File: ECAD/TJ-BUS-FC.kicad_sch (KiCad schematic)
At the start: 19 parts

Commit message: changed fram chip
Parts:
- removed C?: 1uF, symbol Device:C
- removed U?: Adafruit_FRAM, symbol Symbols:Adafruit_FRAM
- added C?: (no value), symbol Device:C
- added J?: PWR, symbol Connector:Conn_01x02_Female
- added U?: (no value), symbol Memory_NVRAM:MB85RS64
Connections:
- net +3V3: no longer U?.2 (3vo)
- net CS/GP37: now also U?.1 (~{CS})
- net GND: now also C?.2, J?.2 (Pin_2), U?.4 (GND)
- net MOSI0: now also U?.5 (SI)
- net SCK0: now also U?.6 (SCK)
- net SCL0: now also U?.5 (SCL)
- net SCL1: no longer U?.5 (SCL)
- net SDA0: now also U?.4 (SDA)
- net SDA1: no longer U?.4 (SDA)
- net 5VIN: now reaches H1.32 (Pin_32)
- net 5VIN: now also J?.1 (Pin_1)
- net at U?.46 (3V3): now also C?.1, U?.8 (VDD)
- new net MOSO0: U?.2 (SO)
- no-connect marks 19 -> 18
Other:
- moved on the sheet: U?

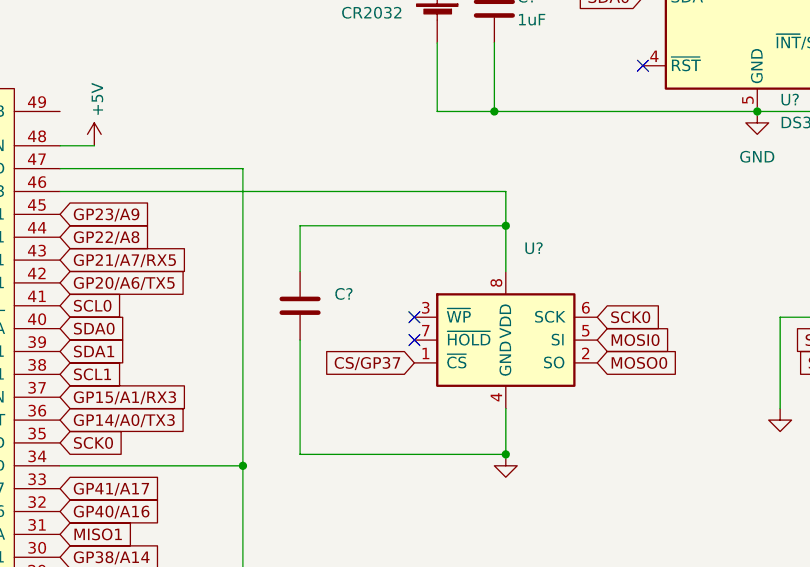
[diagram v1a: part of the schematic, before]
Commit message: set low activated pins to high
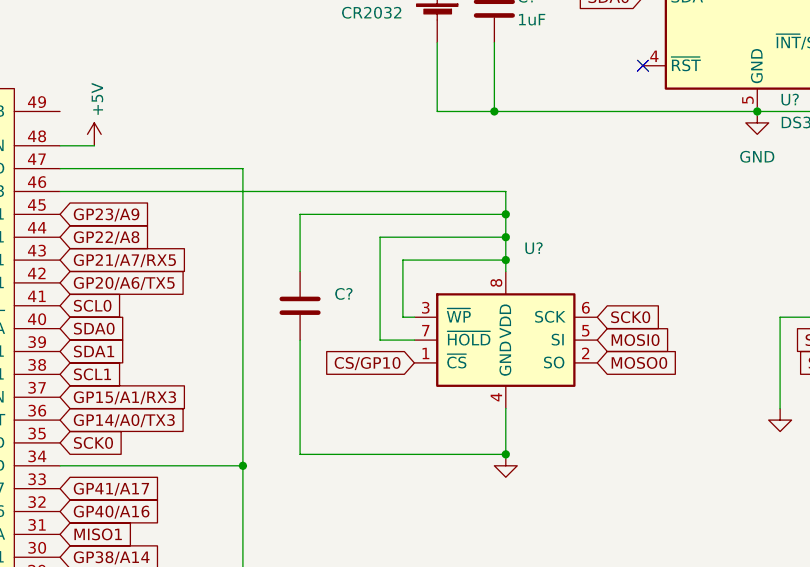
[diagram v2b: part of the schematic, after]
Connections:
- net CS/GP10: now also U?.1 (~{CS})
- net CS/GP37: no longer U?.1 (~{CS})
- net at U?.3 (~{WP}): now also C?.1, U?.46 (3V3), U?.7 (~{HOLD}), U?.8 (VDD)
- no-connect marks 18 -> 16
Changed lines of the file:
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@@
 (kicad_sch (version 20211123) (generator eeschema)
   (paper "USLegal")
-  (junction (at 165.1 64.77) (diameter 0) (color 0 0 0 0)
+  (junction (at 165.1 63.5) (diameter 0) (color 0 0 0 0)
+  )
+  (junction (at 165.1 66.04) (diameter 0) (color 0 0 0 0)
   )
   (junction (at 336.55 86.36) (diameter 0) (color 0 0 0 0)
@@
   )
   (junction (at 306.07 86.36) (diameter 0) (color 0 0 0 0)
+  )
+  (junction (at 165.1 68.58) (diameter 0) (color 0 0 0 0)
   )
   (junction (at 193.04 52.07) (diameter 0) (color 0 0 0 0)
@@
   (no_connect (at 204.47 72.39))
   (no_connect (at 224.79 80.01))
-  (no_connect (at 154.94 74.93))
   (no_connect (at 224.79 74.93))
   (no_connect (at 224.79 72.39))
@@
   (no_connect (at 327.66 96.52))
   (no_connect (at 327.66 76.2))
-  (no_connect (at 154.94 77.47))
   (wire (pts (xy 115.57 123.19) (xy 135.89 123.19))
     (stroke (width 0) (type default) (color 0 0 0 0))
   )
+  (wire (pts (xy 153.67 68.58) (xy 153.67 74.93))
+    (stroke (width 0) (type default) (color 0 0 0 0))
+  )
   (wire (pts (xy 163.83 31.75) (xy 163.83 36.83))
     (stroke (width 0) (type default) (color 0 0 0 0))
@@
     (stroke (width 0) (type default) (color 0 0 0 0))
   )
+  (wire (pts (xy 165.1 68.58) (xy 165.1 69.85))
+    (stroke (width 0) (type default) (color 0 0 0 0))
+  )
   (wire (pts (xy 157.48 52.07) (xy 163.83 52.07))
     (stroke (width 0) (type default) (color 0 0 0 0))
   )
+  (wire (pts (xy 165.1 66.04) (xy 165.1 68.58))
+    (stroke (width 0) (type default) (color 0 0 0 0))
+  )
   (wire (pts (xy 41.91 55.88) (xy 41.91 133.35))
     (stroke (width 0) (type default) (color 0 0 0 0))
@@
     (stroke (width 0) (type default) (color 0 0 0 0))
   )
+  (wire (pts (xy 151.13 66.04) (xy 151.13 77.47))
+    (stroke (width 0) (type default) (color 0 0 0 0))
+  )
   (wire (pts (xy 306.07 83.82) (xy 314.96 83.82))
     (stroke (width 0) (type default) (color 0 0 0 0))
@@
     (stroke (width 0) (type default) (color 0 0 0 0))
   )
+  (wire (pts (xy 154.94 74.93) (xy 153.67 74.93))
+    (stroke (width 0) (type default) (color 0 0 0 0))
+  )
   (wire (pts (xy 115.57 60.96) (xy 165.1 60.96))
     (stroke (width 0) (type default) (color 0 0 0 0))
@@
     (stroke (width 0) (type default) (color 0 0 0 0))
   )
-  (wire (pts (xy 165.1 60.96) (xy 165.1 64.77))
+  (wire (pts (xy 165.1 60.96) (xy 165.1 63.5))
     (stroke (width 0) (type default) (color 0 0 0 0))
   )
@@
     (stroke (width 0) (type default) (color 0 0 0 0))
   )
-  (wire (pts (xy 165.1 64.77) (xy 165.1 69.85))
+  (wire (pts (xy 165.1 63.5) (xy 165.1 66.04))
+    (stroke (width 0) (type default) (color 0 0 0 0))
+  )
+  (wire (pts (xy 153.67 68.58) (xy 165.1 68.58))
     (stroke (width 0) (type default) (color 0 0 0 0))
   )
@@
     (stroke (width 0) (type default) (color 0 0 0 0))
   )
+  (wire (pts (xy 151.13 77.47) (xy 154.94 77.47))
+    (stroke (width 0) (type default) (color 0 0 0 0))
+  )
   (wire (pts (xy 165.1 85.09) (xy 165.1 90.17))
     (stroke (width 0) (type default) (color 0 0 0 0))
@@
     (stroke (width 0) (type default) (color 0 0 0 0))
   )
+  (wire (pts (xy 165.1 66.04) (xy 151.13 66.04))
+    (stroke (width 0) (type default) (color 0 0 0 0))
+  )
   (wire (pts (xy 163.83 31.75) (xy 157.48 31.75))
     (stroke (width 0) (type default) (color 0 0 0 0))
   )
-  (wire (pts (xy 142.24 64.77) (xy 165.1 64.77))
-    (stroke (width 0) (type default) (color 0 0 0 0))
-  )
-  (wire (pts (xy 142.24 69.85) (xy 142.24 64.77))
+  (wire (pts (xy 142.24 63.5) (xy 165.1 63.5))
+    (stroke (width 0) (type default) (color 0 0 0 0))
+  )
+  (wire (pts (xy 142.24 69.85) (xy 142.24 63.5))
     (stroke (width 0) (type default) (color 0 0 0 0))
   )
@@
     )
   )
-  (global_label "CS{slash}GP37" (shape input) (at 154.94 80.01 180) (fields_autoplaced)
+  (global_label "CS{slash}GP10" (shape input) (at 154.94 80.01 180) (fields_autoplaced)
     (effects (font (size 1.27 1.27)) (justify right))
     (property "Intersheet References" "${INTERSHEET_REFS}" (id 0) (at 143.8468 79.9306 0)

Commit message: minor nitpicks
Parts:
- removed J?: PWR, symbol Connector:Conn_01x02_Female
- U?: value (none) -> MB85RS64
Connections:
- net 5VIN: no longer names the net of H1.32 (Pin_32)
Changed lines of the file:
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@@
 (kicad_sch (version 20211123) (generator eeschema)
   (paper "USLegal")
-  (junction (at 165.1 63.5) (diameter 0) (color 0 0 0 0)
-  )
-  (junction (at 165.1 66.04) (diameter 0) (color 0 0 0 0)
-  )
   (junction (at 336.55 86.36) (diameter 0) (color 0 0 0 0)
   )
   (junction (at 165.1 90.17) (diameter 0) (color 0 0 0 0)
   )
+  (junction (at 151.13 74.93) (diameter 0) (color 0 0 0 0)
+  )
   (junction (at 163.83 31.75) (diameter 0) (color 0 0 0 0)
   )
@@
   (junction (at 306.07 86.36) (diameter 0) (color 0 0 0 0)
   )
-  (junction (at 165.1 68.58) (diameter 0) (color 0 0 0 0)
+  (junction (at 142.24 60.96) (diameter 0) (color 0 0 0 0)
   )
   (junction (at 193.04 52.07) (diameter 0) (color 0 0 0 0)
+  )
+  (junction (at 151.13 60.96) (diameter 0) (color 0 0 0 0)
   )
   (no_connect (at 314.96 93.98))
@@
     (stroke (width 0) (type default) (color 0 0 0 0))
   )
-  (wire (pts (xy 153.67 68.58) (xy 153.67 74.93))
+  (wire (pts (xy 151.13 74.93) (xy 151.13 77.47))
     (stroke (width 0) (type default) (color 0 0 0 0))
   )
@@
     (stroke (width 0) (type default) (color 0 0 0 0))
   )
-  (wire (pts (xy 165.1 68.58) (xy 165.1 69.85))
-    (stroke (width 0) (type default) (color 0 0 0 0))
-  )
   (wire (pts (xy 157.48 52.07) (xy 163.83 52.07))
     (stroke (width 0) (type default) (color 0 0 0 0))
   )
-  (wire (pts (xy 165.1 66.04) (xy 165.1 68.58))
-    (stroke (width 0) (type default) (color 0 0 0 0))
-  )
   (wire (pts (xy 41.91 55.88) (xy 41.91 133.35))
     (stroke (width 0) (type default) (color 0 0 0 0))
@@
     (stroke (width 0) (type default) (color 0 0 0 0))
   )
+  (wire (pts (xy 142.24 60.96) (xy 151.13 60.96))
+    (stroke (width 0) (type default) (color 0 0 0 0))
+  )
   (wire (pts (xy 306.07 86.36) (xy 314.96 86.36))
     (stroke (width 0) (type default) (color 0 0 0 0))
@@
     (stroke (width 0) (type default) (color 0 0 0 0))
   )
-  (wire (pts (xy 151.13 66.04) (xy 151.13 77.47))
+  (wire (pts (xy 151.13 60.96) (xy 151.13 74.93))
     (stroke (width 0) (type default) (color 0 0 0 0))
   )
@@
     (stroke (width 0) (type default) (color 0 0 0 0))
   )
-  (wire (pts (xy 154.94 74.93) (xy 153.67 74.93))
-    (stroke (width 0) (type default) (color 0 0 0 0))
-  )
-  (wire (pts (xy 115.57 60.96) (xy 165.1 60.96))
+  (wire (pts (xy 151.13 74.93) (xy 154.94 74.93))
+    (stroke (width 0) (type default) (color 0 0 0 0))
+  )
+  (wire (pts (xy 115.57 60.96) (xy 142.24 60.96))
+    (stroke (width 0) (type default) (color 0 0 0 0))
+  )
+  (wire (pts (xy 151.13 60.96) (xy 165.1 60.96))
     (stroke (width 0) (type default) (color 0 0 0 0))
   )
@@
     (stroke (width 0) (type default) (color 0 0 0 0))
   )
-  (wire (pts (xy 165.1 60.96) (xy 165.1 63.5))
+  (wire (pts (xy 165.1 60.96) (xy 165.1 69.85))
     (stroke (width 0) (type default) (color 0 0 0 0))
   )
@@
     (stroke (width 0) (type default) (color 0 0 0 0))
   )
-  (wire (pts (xy 165.1 63.5) (xy 165.1 66.04))
-    (stroke (width 0) (type default) (color 0 0 0 0))
-  )
-  (wire (pts (xy 153.67 68.58) (xy 165.1 68.58))
-    (stroke (width 0) (type default) (color 0 0 0 0))
-  )
   (wire (pts (xy 157.48 31.75) (xy 157.48 36.83))
     (stroke (width 0) (type default) (color 0 0 0 0))
@@
     (stroke (width 0) (type default) (color 0 0 0 0))
   )
-  (wire (pts (xy 165.1 66.04) (xy 151.13 66.04))
-    (stroke (width 0) (type default) (color 0 0 0 0))
-  )
   (wire (pts (xy 163.83 31.75) (xy 157.48 31.75))
     (stroke (width 0) (type default) (color 0 0 0 0))
   )
-  (wire (pts (xy 142.24 63.5) (xy 165.1 63.5))
-    (stroke (width 0) (type default) (color 0 0 0 0))
-  )
-  (wire (pts (xy 142.24 69.85) (xy 142.24 63.5))
+  (wire (pts (xy 142.24 60.96) (xy 142.24 69.85))
     (stroke (width 0) (type default) (color 0 0 0 0))
   )
@@
     )
   )
-  (global_label "5VIN" (shape input) (at 224.79 135.89 180) (fields_autoplaced)
-    (effects (font (size 1.27 1.27)) (justify right))
-    (property "Intersheet References" "${INTERSHEET_REFS}" (id 0) (at 462.28 220.98 0)
-      (effects (font (size 1.27 1.27)) hide)
-    )
-  )
   (global_label "RX2{slash}GP7" (shape input) (at 279.4 58.42 180) (fields_autoplaced)
     (effects (font (size 1.27 1.27)) (justify right))
@@
     (property "Intersheet References" "${INTERSHEET_REFS}" (id 0) (at 304.2213 78.6606 0)
       (effects (font (size 1.27 1.27)) (justify left) hide)
-    )
-  )
-  (global_label "5VIN" (shape input) (at 292.1 86.36 0) (fields_autoplaced)
-    (effects (font (size 1.27 1.27)) (justify left))
-    (property "Intersheet References" "${INTERSHEET_REFS}" (id 0) (at 54.61 1.27 0)
-      (effects (font (size 1.27 1.27)) hide)
     )
   )
@@
       (effects (font (size 1.27 1.27)) hide)
     )
-    (property "Value" "" (id 1) (at 195.58 90.17 0))
+    (property "Value" "GND" (id 1) (at 195.58 90.17 0))
     (property "Footprint" "" (id 2) (at 195.58 85.09 0)
       (effects (font (size 1.27 1.27)) hide)
@@
       (effects (font (size 1.27 1.27)) (justify left))
     )
-    (property "Value" "" (id 1) (at 167.1194 69.85 0)
+    (property "Value" "MB85RS64" (id 1) (at 167.1194 69.85 0)
       (effects (font (size 1.27 1.27)) (justify left))
     )
@@
     (pin "8")
   )
-  (symbol (lib_id "Connector:Conn_01x02_Female") (at 229.87 135.89 0) (unit 1)
-    (in_bom yes) (on_board yes) (fields_autoplaced)
-    (property "Reference" "J?" (id 0) (at 231.14 135.8899 0)
-      (effects (font (size 1.27 1.27)) (justify left))
-    )
-    (property "Value" "PWR" (id 1) (at 231.14 138.4299 0)
-      (effects (font (size 1.27 1.27)) (justify left))
-    )
-    (property "Footprint" "" (id 2) (at 229.87 135.89 0)
-      (effects (font (size 1.27 1.27)) hide)
-    )
-    (property "Datasheet" "~" (id 3) (at 229.87 135.89 0)
-      (effects (font (size 1.27 1.27)) hide)
-    )
-    (pin "1")
-    (pin "2")
-  )
   (symbol (lib_id "power:GND") (at 193.04 52.07 0) (unit 1)
     (in_bom yes) (on_board yes)
@@
     (pin "1")
   )
-  (symbol (lib_id "power:GND") (at 224.79 138.43 0) (unit 1)
-    (in_bom yes) (on_board yes) (fields_autoplaced)
-    (property "Reference" "#PWR?" (id 0) (at 224.79 144.78 0)
-      (effects (font (size 1.27 1.27)) hide)
-    )
-    (property "Value" "GND" (id 1) (at 224.79 143.51 0))
-    (property "Footprint" "" (id 2) (at 224.79 138.43 0)
-      (effects (font (size 1.27 1.27)) hide)
-    )
-    (property "Datasheet" "" (id 3) (at 224.79 138.43 0)
-      (effects (font (size 1.27 1.27)) hide)
-    )
-    (pin "1")
-  )
   (symbol (lib_id "Device:C") (at 163.83 40.64 0) (unit 1)
     (in_bom yes) (on_board yes)
@@
       (effects (font (size 1.27 1.27)) hide)
     )
-    (property "Value" "" (id 1) (at 165.1 95.25 0))
+    (property "Value" "GND" (id 1) (at 165.1 95.25 0))
     (property "Footprint" "" (id 2) (at 165.1 90.17 0)
       (effects (font (size 1.27 1.27)) hide)
@@
   )
   (symbol (lib_id "Device:C") (at 142.24 73.66 0) (unit 1)
-    (in_bom yes) (on_board yes) (fields_autoplaced)
-    (property "Reference" "C?" (id 0) (at 146.05 72.3899 0)
-      (effects (font (size 1.27 1.27)) (justify left))
-    )
-    (property "Value" "" (id 1) (at 146.05 74.9299 0)
+    (in_bom yes) (on_board yes)
+    (property "Reference" "C?" (id 0) (at 144.78 72.39 0)
+      (effects (font (size 1.27 1.27)) (justify left))
+    )
+    (property "Value" "" (id 1) (at 144.78 74.93 0)
       (effects (font (size 1.27 1.27)) (justify left))
     )
@@
       (effects (font (size 1.27 1.27)) hide)
     )
-    (property "Value" "" (id 1) (at 200.66 69.8499 90)
+    (property "Value" "+3.3V" (id 1) (at 200.66 69.8499 90)
       (effects (font (size 1.27 1.27)) (justify left))
     )
@@
       (reference "#PWR?") (unit 1) (value "GND") (footprint "")
     )
-    (path "/ada2bafc-40cb-4d29-9269-ce160ab48fcc"
-      (reference "#PWR?") (unit 1) (value "GND") (footprint "")
-    )
     (path "/1b0ebad7-8a43-40a6-b997-58eed2589c95/ba16728d-3684-42ae-a4d8-298c4a006593"
       (reference "#PWR?") (unit 1) (value "GND") (footprint "")
@@
     )
     (path "/be5f9a77-0429-4df0-92dd-b6e55cb3b5d6"
-      (reference "C?") (unit 1) (value "1uF") (footprint "")
+      (reference "C?") (unit 1) (value "0.1uF") (footprint "")
     )
     (path "/1b0ebad7-8a43-40a6-b997-58eed2589c95/c8117bba-6b2a-4528-9104-16037ce7eb42"
@@
       (reference "H2") (unit 1) (value "Stack Header") (footprint "Connector_PinHeader_2.54mm:PinHeader_2x26_P2.54mm_Vertical")
     )
-    (path "/8142001c-a9d5-457a-9968-95120d035d39"
-      (reference "J?") (unit 1) (value "PWR") (footprint "")
-    )
     (path "/1b0ebad7-8a43-40a6-b997-58eed2589c95/2c8c9572-9c16-41b9-81dc-5ea6c5fa6361"

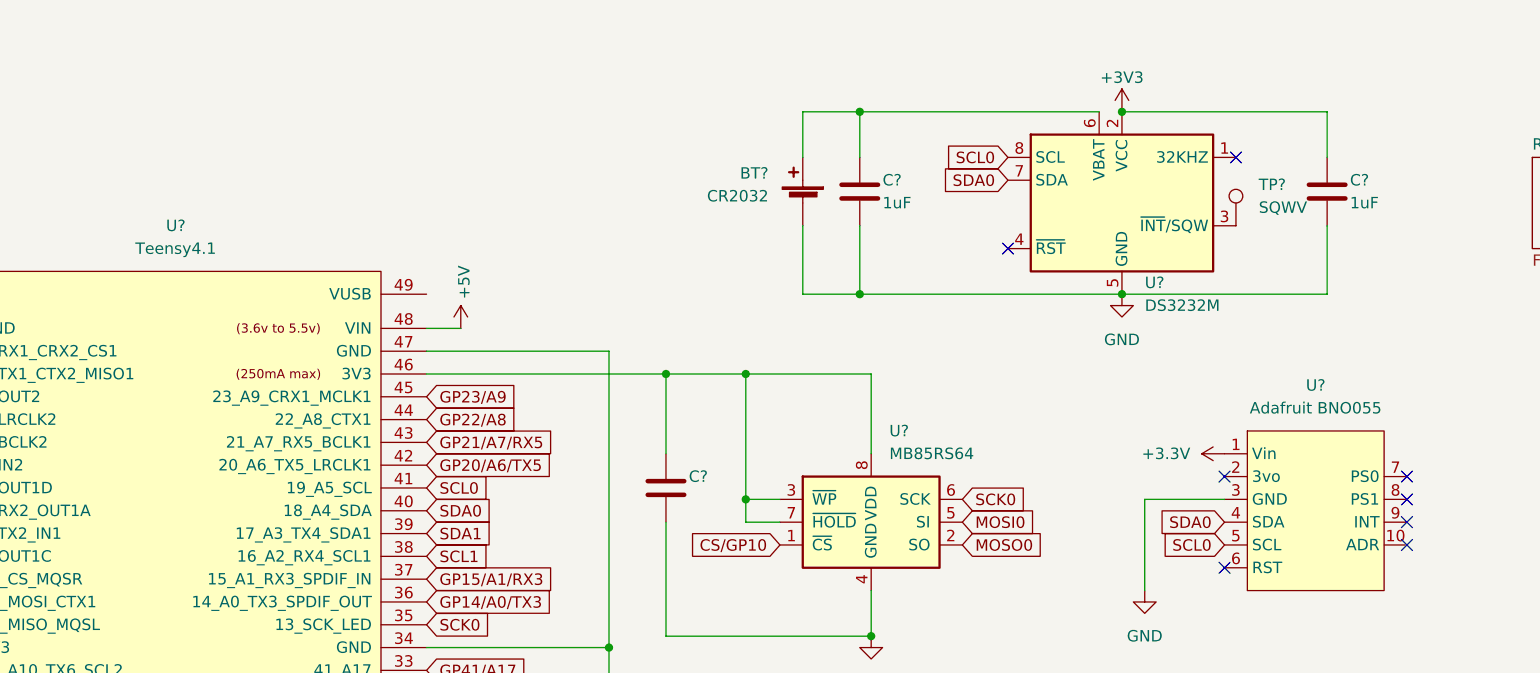
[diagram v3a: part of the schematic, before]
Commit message: add footprints and update iridium section
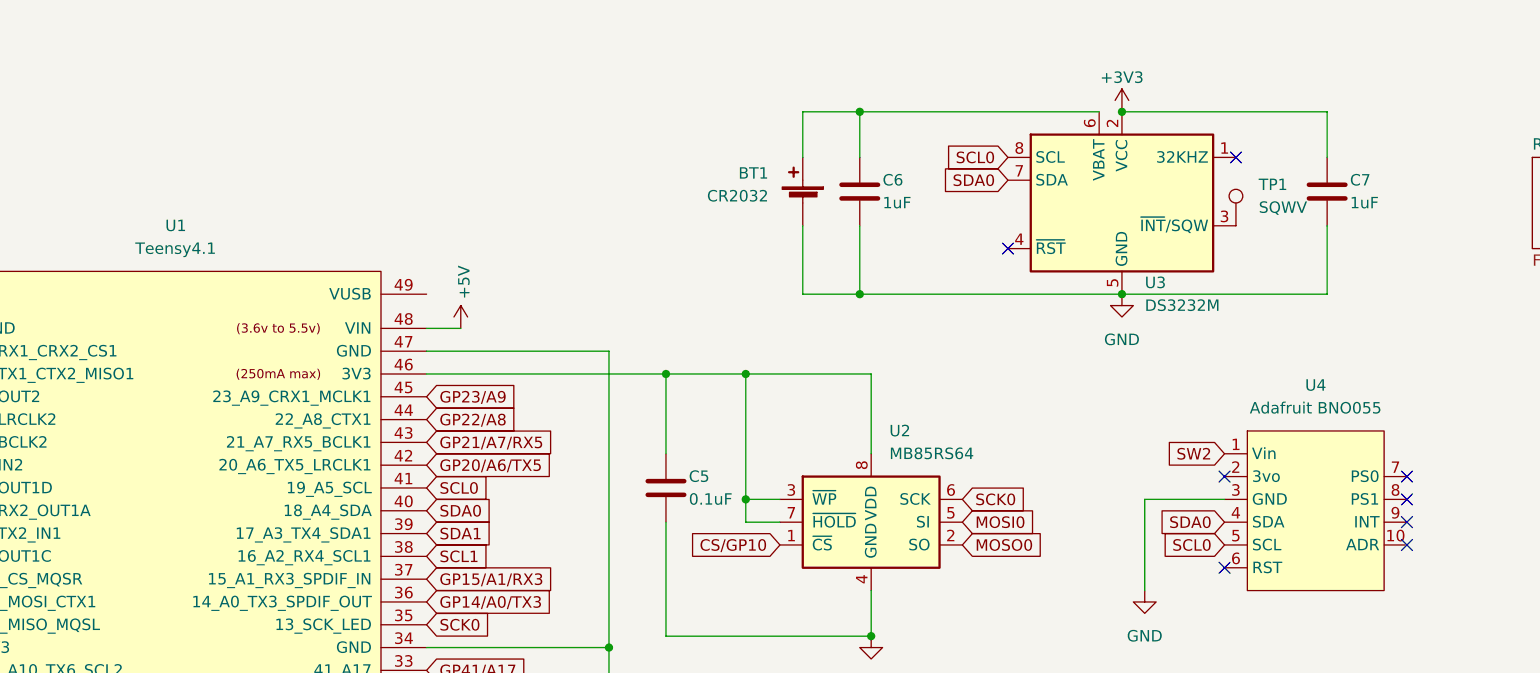
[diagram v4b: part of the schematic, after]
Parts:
- C5: renamed from C?; value (none) -> 0.1uF
- gave numbers to parts that had none: 8
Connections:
- net +3V3: no longer U4.1 (Vin)
- net SW2: now also U4.1 (Vin)
